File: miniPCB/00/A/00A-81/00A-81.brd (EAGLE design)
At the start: 49.7 x 42 mm, 1 part

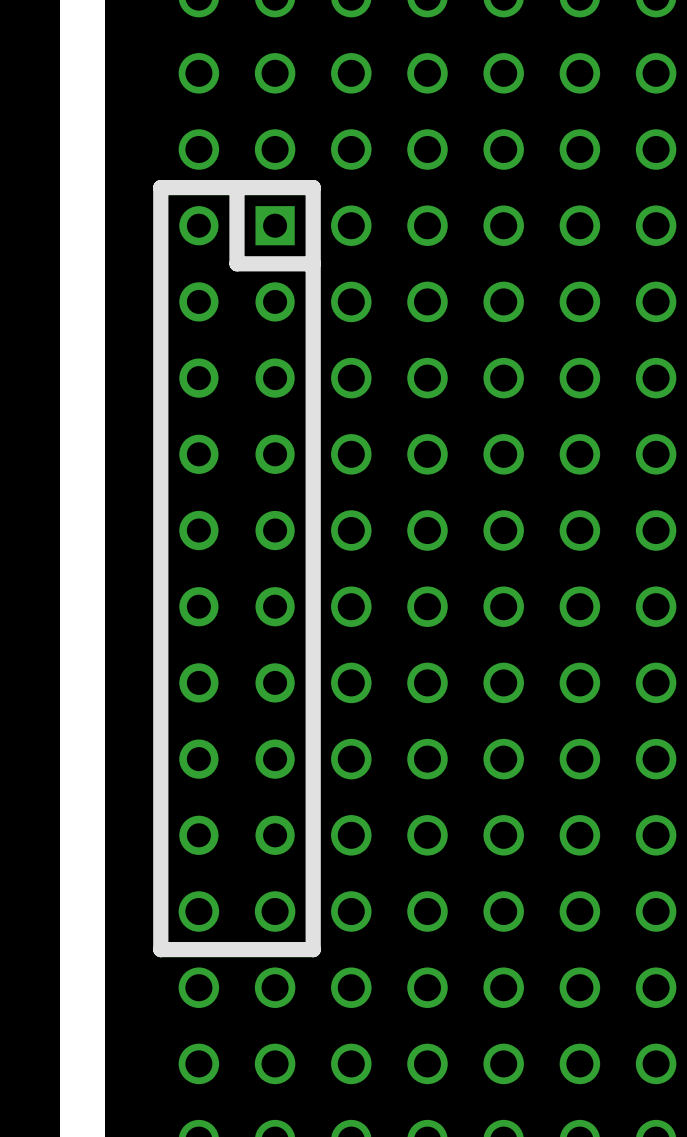
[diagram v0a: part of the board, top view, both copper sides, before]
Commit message: Giving vScore boards regular part numbers
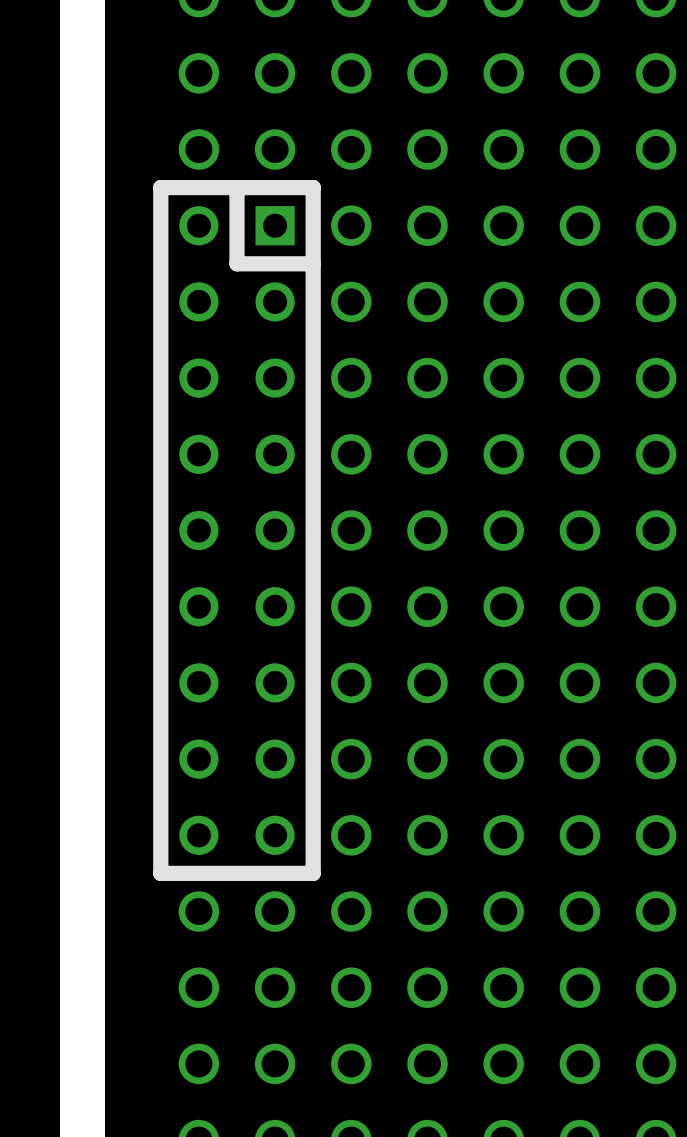
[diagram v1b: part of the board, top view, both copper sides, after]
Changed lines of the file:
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@@
 <setting verticaltext="up"/>
 </settings>
-<grid distance="0.01" unitdist="inch" unit="inch" style="lines" multiple="1" display="yes" altdistance="0.025" altunitdist="inch" altunit="inch"/>
+<grid distance="0.1" unitdist="inch" unit="inch" style="lines" multiple="1" display="yes" altdistance="0.025" altunitdist="inch" altunit="inch"/>
 <layers>
 <layer number="1" name="Top" color="4" fill="1" visible="yes" active="yes"/>
@@
 <plain>
 <wire x1="3.81" y1="1.27" x2="3.81" y2="-1.27" width="0.508" layer="21"/>
-<wire x1="3.81" y1="-1.27" x2="3.81" y2="-24.13" width="0.508" layer="21"/>
-<wire x1="3.81" y1="-24.13" x2="-1.27" y2="-24.13" width="0.508" layer="21"/>
-<wire x1="-1.27" y1="-24.13" x2="-1.27" y2="1.27" width="0.508" layer="21"/>
+<wire x1="3.81" y1="-1.27" x2="3.81" y2="-21.59" width="0.508" layer="21"/>
+<wire x1="3.81" y1="-21.59" x2="-1.27" y2="-21.59" width="0.508" layer="21"/>
+<wire x1="-1.27" y1="-21.59" x2="-1.27" y2="1.27" width="0.508" layer="21"/>
 <wire x1="-1.27" y1="1.27" x2="1.27" y2="1.27" width="0.508" layer="21"/>
 <wire x1="1.27" y1="1.27" x2="3.81" y2="1.27" width="0.508" layer="21"/>
